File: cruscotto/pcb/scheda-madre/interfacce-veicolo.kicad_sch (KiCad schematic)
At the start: 23 parts, among them Q8 MMBT5551, U7 LM2903B, U8 SN65HVD230, U9 AP2112K-3.3

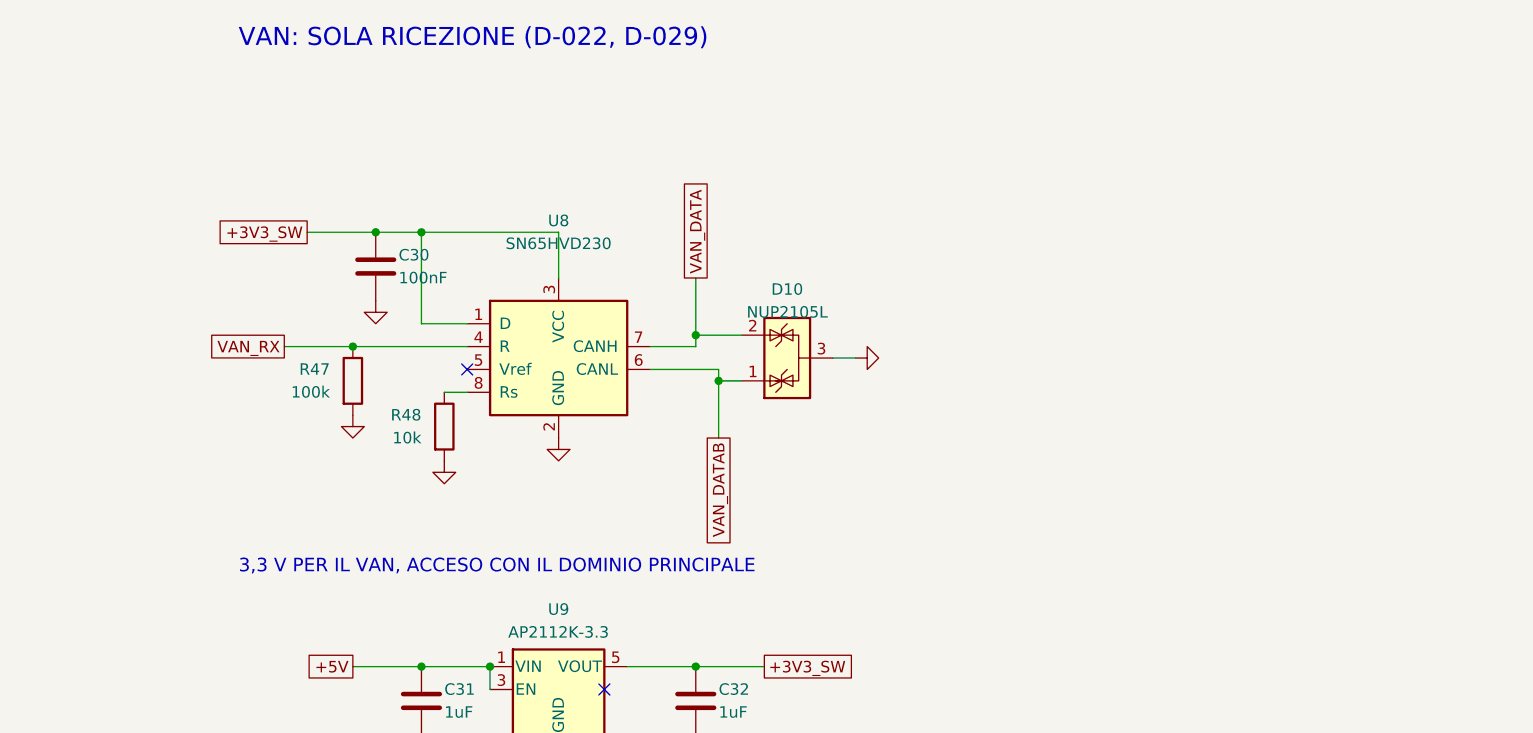
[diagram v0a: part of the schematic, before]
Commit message: feat(schematic): D-051 mixed approach, VAN and MicroSD as modules on pin headers, RTC stays a chip
CR-EL-003 rev B: blue SN65HVD230 module on J8/J9 headers with TX tied high on the board, NUP2105L kept. CR-EL-004 rev B: MicroSD reader module on a 6-way header, CS pull-up and bulk caps. Inventory: second module units needed for the mainboard, header spacing to measure. ERC: 0 errors; 88 nets checked.

Co-Authored-By: Claude Opus 5.5 <noreply@anthropic.com>
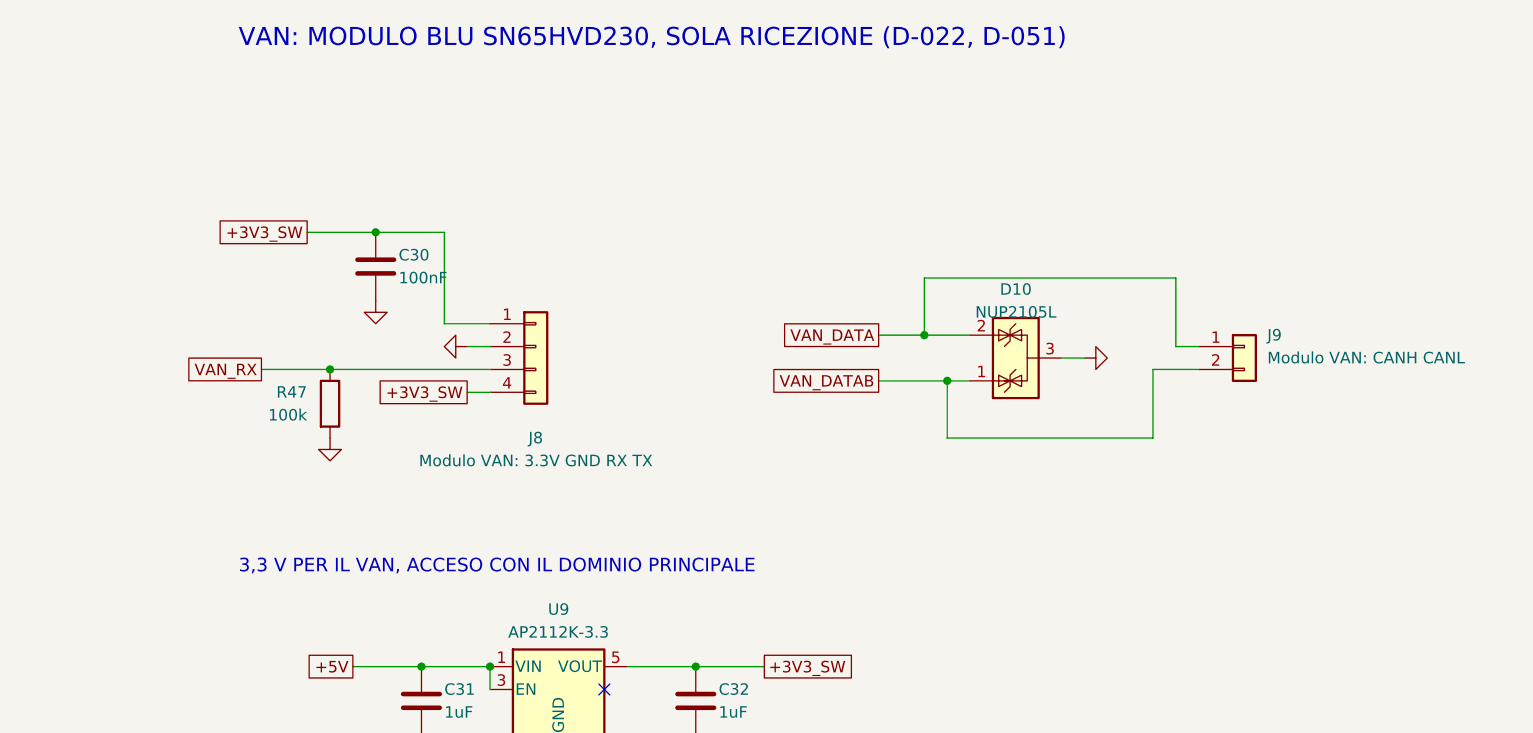
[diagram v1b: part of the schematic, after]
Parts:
- removed R48: 10k, Resistor_SMD:R_0805_2012Metric_Pad1.20x1.40mm_HandSolder, symbol Device:R
- removed U8: SN65HVD230, Package_SO:SOIC-8_3.9x4.9mm_P1.27mm, symbol Interface_CAN_LIN:SN65HVD230
- added J8: Modulo VAN: 3.3V GND RX TX, Connector_PinHeader_2.54mm:PinHeader_1x04_P2.54mm_Vertical, symbol Connector_Generic:Conn_01x04
- added J9: Modulo VAN: CANH CANL, Connector_PinHeader_2.54mm:PinHeader_1x02_P2.54mm_Vertical, symbol Connector_Generic:Conn_01x02
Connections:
- net +3V3_SW: now also J8.1 (Pin_1), J8.4 (Pin_4)
- net GND: now also J8.2 (Pin_2)
- net VAN_DATA: now also J9.1 (Pin_1)
- net VAN_DATAB: now also J9.2 (Pin_2)
- net VAN_RX: now also J8.3 (Pin_3)
- no-connect marks 3 -> 2
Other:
- note added: "VAN: MODULO BLU SN65HVD230, SOLA RICEZIONE (D-022, D-051)"
- note removed: "VAN: SOLA RICEZIONE (D-022, D-029)"
- moved on the sheet: D10, R47

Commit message: feat(pcb): D-060 VAN module soldered flat on the back, re-routed; 3D envelopes with fan for the STEP
- D-060: VAN module footprint Modulo_VAN_SN65HVD230 (4 straight pins on J8, 35 x 13 mm body on the
  back, over the U4 thermal vias: mount after U4); CANH/CANL by two wires from the module screw
  terminal to J9 pads. J8 and J9 were wrongly placed as two separate connectors 53 mm apart.
  Schematic EL-003 rev C. Generator: body on one side only for J8 and U4 (thermal vias kept free).
- completa-sbroglio: stuck nets may also rip up nearby power tracks (not ground).
- Board: 5653 tracks, 566 vias; DRC 0 violations including warnings, 0 unconnected.
- tools/modelli-3d-scheda-madre.py: STEP envelope boxes for parts without KiCad models (relays,
  C3 17.5 mm, J1, USB-C, U2, STEVAL, VAN module) and the Delta fan 40 x 40 x 10 on the back (VENT1,
  mechanical only). Silkscreen, assembly drawings, assembly list and previews regenerated.

Co-Authored-By: Claude Opus 5.5 <noreply@anthropic.com>
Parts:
- J8: footprint Connector_PinHeader_2.54mm:PinHeader_1x04_P2.54mm_Vertical -> scheda-madre:Modulo_VAN_SN65HVD230
- J9: footprint Connector_PinHeader_2.54mm:PinHeader_1x02_P2.54mm_Vertical -> Connector_Wire:SolderWire-0.127sqmm_1x02_P3.7mm_D0.48mm_OD1mm
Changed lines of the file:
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@@
 	(title_block
 		(title "Scheda madre cruscotto C3+AI - interfacce veicolo")
-		(date "2026-10-24")
-		(rev "B")
+		(date "2026-10-28")
+		(rev "C")
 		(company "Cruscotto C3+AI")
-		(comment 1 "C3AI-CR-EL-003 rev B - proposta preliminare, non verificata")
-		(comment 2 "D-008, D-022, D-029, D-033, D-046, D-051")
+		(comment 1 "C3AI-CR-EL-003 rev C - proposta preliminare, non verificata")
+		(comment 2 "D-008, D-022, D-029, D-033, D-046, D-051, D-060")
 		(comment 3 "Generato da tools/genera-schema-scheda-madre.py")
 	)
@@
 		(property "Reference" "J8" (at 231.14 76.2 0) (effects (font (size 1.27 1.27))))
 		(property "Value" "Modulo VAN: 3.3V GND RX TX" (at 231.14 78.74 0) (effects (font (size 1.27 1.27))))
-		(property "Footprint" "Connector_PinHeader_2.54mm:PinHeader_1x04_P2.54mm_Vertical" (at 231.14 66.04 0) (hide yes) (effects (font (size 1.27 1.27))))
+		(property "Footprint" "scheda-madre:Modulo_VAN_SN65HVD230" (at 231.14 66.04 0) (hide yes) (effects (font (size 1.27 1.27))))
 		(property "Datasheet" "" (at 231.14 66.04 0) (hide yes) (effects (font (size 1.27 1.27))))
 		(property "Description" "Modulo con resistenza 121 rimossa (VAN-M002); TX al 3,3 V sulla scheda: trasmettitore sempre recessivo" (at 231.14 66.04 0) (hide yes) (effects (font (size 1.27 1.27))))
@@
 		(property "Reference" "J9" (at 312.42 64.77 0) (effects (font (size 1.27 1.27)) (justify left)))
 		(property "Value" "Modulo VAN: CANH CANL" (at 312.42 67.31 0) (effects (font (size 1.27 1.27)) (justify left)))
-		(property "Footprint" "Connector_PinHeader_2.54mm:PinHeader_1x02_P2.54mm_Vertical" (at 309.88 66.04 0) (hide yes) (effects (font (size 1.27 1.27))))
+		(property "Footprint" "Connector_Wire:SolderWire-0.127sqmm_1x02_P3.7mm_D0.48mm_OD1mm" (at 309.88 66.04 0) (hide yes) (effects (font (size 1.27 1.27))))
 		(property "Datasheet" "" (at 309.88 66.04 0) (hide yes) (effects (font (size 1.27 1.27))))
-		(property "Description" "Interasse con J8 da misurare sul modulo" (at 309.88 66.04 0) (hide yes) (effects (font (size 1.27 1.27))))
-		(pin "1")
-		(pin "2")
+		(property "Description" "Due fili dal morsetto a vite del modulo (D-060)" (at 309.88 66.04 0) (hide yes) (effects (font (size 1.27 1.27))))
+		(pin "1")
+		(pin "2")
